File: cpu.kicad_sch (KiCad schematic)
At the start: 17 parts, among them J1 FTSH-105-01-L-DV-K, U2 CC1312R1F3RGZR, Y2 OW7EL89CANUXK7YLC-48M

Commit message: Finish up inputting things
Signed-off-by: Corey Minyard <corey@minyard.net>
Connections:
- net 144MHz_TX_ENABLE: now reaches U2.28 (DIO_18)
- net 440MHz_TX_ENABLE: now reaches U2.29 (DIO_19)
- no-connect marks 16 -> 14
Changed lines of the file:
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@@
-	)
-	(no_connect
-		(at 78.74 95.25)
 	)
 	(no_connect
@@
 	)
 	(no_connect
-		(at 78.74 97.79)
-	)
-	(no_connect
 		(at 78.74 110.49)
 	)
@@
 	(wire
 		(pts
-			(xy 63.5 123.19) (xy 78.74 123.19)
+			(xy 62.23 123.19) (xy 78.74 123.19)
 		)
 		(stroke
@@
 	(wire
 		(pts
+			(xy 59.69 97.79) (xy 78.74 97.79)
+		)
+		(stroke
+			(width 0)
+			(type default)
+		)
+	)
+	(wire
+		(pts
 			(xy 57.15 153.67) (xy 62.23 153.67)
 		)
@@
 		(pts
 			(xy 139.7 52.07) (xy 148.59 52.07)
+		)
+		(stroke
+			(width 0)
+			(type default)
+		)
+	)
+	(wire
+		(pts
+			(xy 59.69 95.25) (xy 78.74 95.25)
 		)
 		(stroke
@@
 		)
 	)
+	(global_label "144MHz_TX_ENABLE"
+		(shape input)
+		(at 59.69 95.25 180)
+		(fields_autoplaced yes)
+		(effects
+			(font
+				(size 1.27 1.27)
+			)
+			(justify right)
+		)
+		(property "Intersheetrefs" "${INTERSHEET_REFS}"
+			(at 38.1388 95.25 0)
+			(effects
+				(font
+					(size 1.27 1.27)
+				)
+				(justify right)
+				(hide yes)
+			)
+		)
+	)
 	(global_label "144MHz_RF_P"
 		(shape input)
@@
 	(global_label "RADIO2_TCXO_POW"
 		(shape input)
-		(at 63.5 123.19 180)
+		(at 62.23 123.19 180)
 		(fields_autoplaced yes)
 		(effects
@@
 		)
 		(property "Intersheetrefs" "${INTERSHEET_REFS}"
-			(at 42.9767 123.19 0)
+			(at 41.7067 123.19 0)
 			(effects
 				(font
@@
 		(property "Intersheetrefs" "${INTERSHEET_REFS}"
 			(at 41.8882 85.09 0)
+			(effects
+				(font
+					(size 1.27 1.27)
+				)
+				(justify right)
+				(hide yes)
+			)
+		)
+	)
+	(global_label "440MHz_TX_ENABLE"
+		(shape input)
+		(at 59.69 97.79 180)
+		(fields_autoplaced yes)
+		(effects
+			(font
+				(size 1.27 1.27)
+			)
+			(justify right)
+		)
+		(property "Intersheetrefs" "${INTERSHEET_REFS}"
+			(at 38.1388 97.79 0)
 			(effects
 				(font
@@
 		(dnp no)
 		(property "Reference" "C8"
-			(at 150.876 131.826 90)
+			(at 153.416 129.54 90)
 			(effects
 				(font
@@
 		)
 		(property "Value" "1nF"
-			(at 160.02 132.08 90)
-			(effects
-				(font
+			(at 154.432 137.414 90)
+			(effects
+				(font

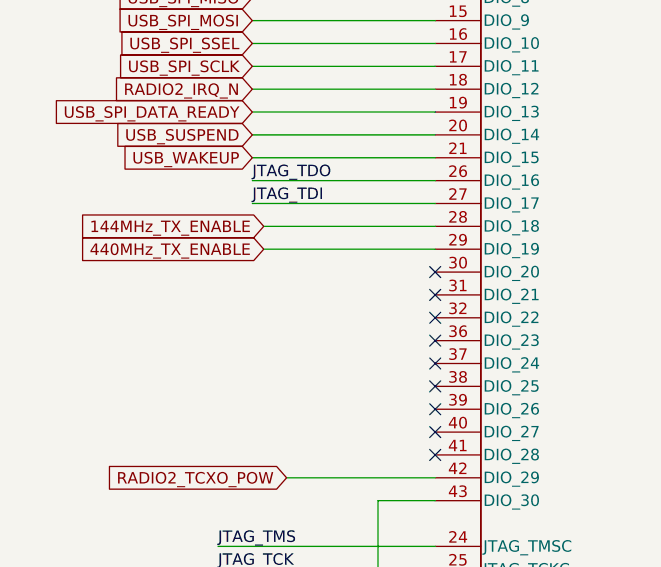
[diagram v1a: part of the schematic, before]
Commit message: Clean up schematics
Signed-off-by: Corey Minyard <corey@minyard.net>
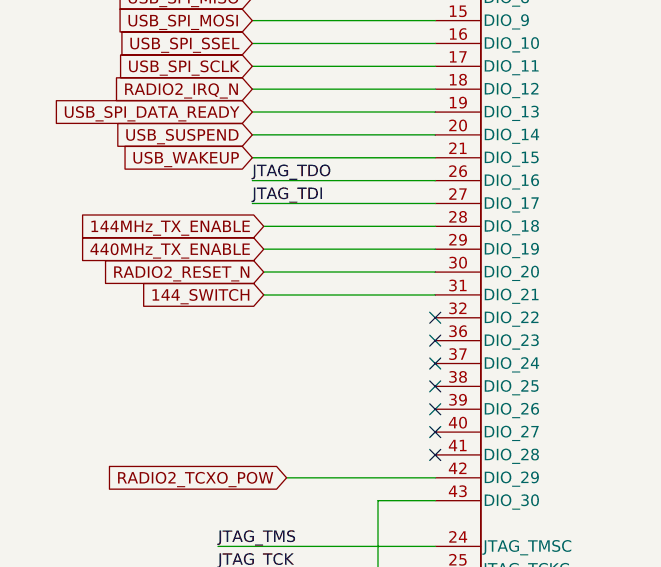
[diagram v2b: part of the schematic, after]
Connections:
- net RADIO2_RESET_N: now reaches U2.30 (DIO_20)
- net 144_SWITCH: now reaches U2.31 (DIO_21)
- no-connect marks 14 -> 12
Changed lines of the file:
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@@
 	)
 	(no_connect
-		(at 78.74 100.33)
-	)
-	(no_connect
 		(at 139.7 162.56)
 	)
@@
 	)
 	(no_connect
-		(at 78.74 102.87)
-	)
-	(no_connect
 		(at 78.74 115.57)
 	)
@@
 	(wire
 		(pts
+			(xy 59.69 102.87) (xy 78.74 102.87)
+		)
+		(stroke
+			(width 0)
+			(type default)
+		)
+	)
+	(wire
+		(pts
 			(xy 165.1 69.85) (xy 182.88 69.85)
 		)
@@
 	(wire
 		(pts
+			(xy 59.69 100.33) (xy 78.74 100.33)
+		)
+		(stroke
+			(width 0)
+			(type default)
+		)
+	)
+	(wire
+		(pts
 			(xy 58.42 67.31) (xy 78.74 67.31)
 		)
@@
 		)
 	)
+	(global_label "RADIO2_RESET_N"
+		(shape input)
+		(at 59.69 100.33 180)
+		(fields_autoplaced yes)
+		(effects
+			(font
+				(size 1.27 1.27)
+			)
+			(justify right)
+		)
+		(property "Intersheetrefs" "${INTERSHEET_REFS}"
+			(at 40.9206 100.33 0)
+			(effects
+				(font
+					(size 1.27 1.27)
+				)
+				(justify right)
+				(hide yes)
+			)
+		)
+	)
 	(global_label "USB_SPI_MOSI"
 		(shape input)
@@
 		)
 	)
+	(global_label "144_SWITCH"
+		(shape input)
+		(at 59.69 102.87 180)
+		(fields_autoplaced yes)
+		(effects
+			(font
+				(size 1.27 1.27)
+			)
+			(justify right)
+		)
+		(property "Intersheetrefs" "${INTERSHEET_REFS}"
+			(at 45.2749 102.87 0)
+			(effects
+				(font
+					(size 1.27 1.27)
+				)
+				(justify right)
+				(hide yes)
+			)
+		)
+	)
 	(global_label "USB_WAKEUP"
 		(shape input)
@@
 		(pin "22"
 		)
+		(instances
+			(project ""
+				(path "/23e49ab9-97e0-460a-806c-ff6f37958474/f1de8cbf-f219-47ea-9542-15169289ddba"
+					(reference "U2")
+					(unit 1)
+				)
+			)
+		)
 	)

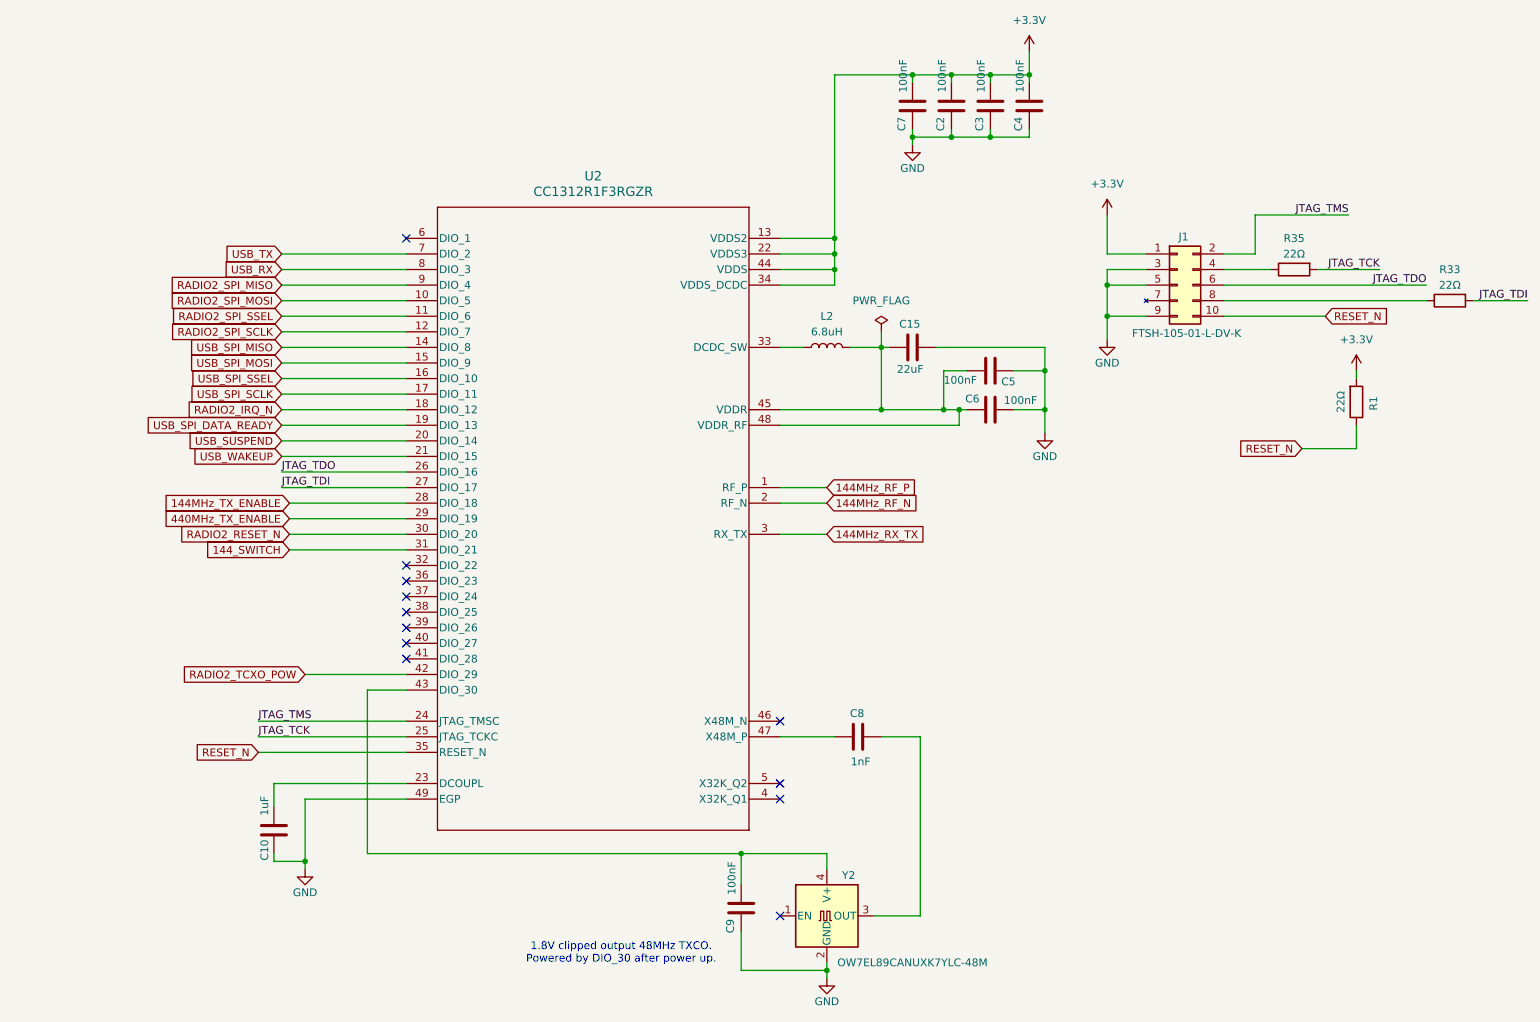
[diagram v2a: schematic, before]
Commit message: More cleanups and add some test points
Signed-off-by: Corey Minyard <corey@minyard.net>
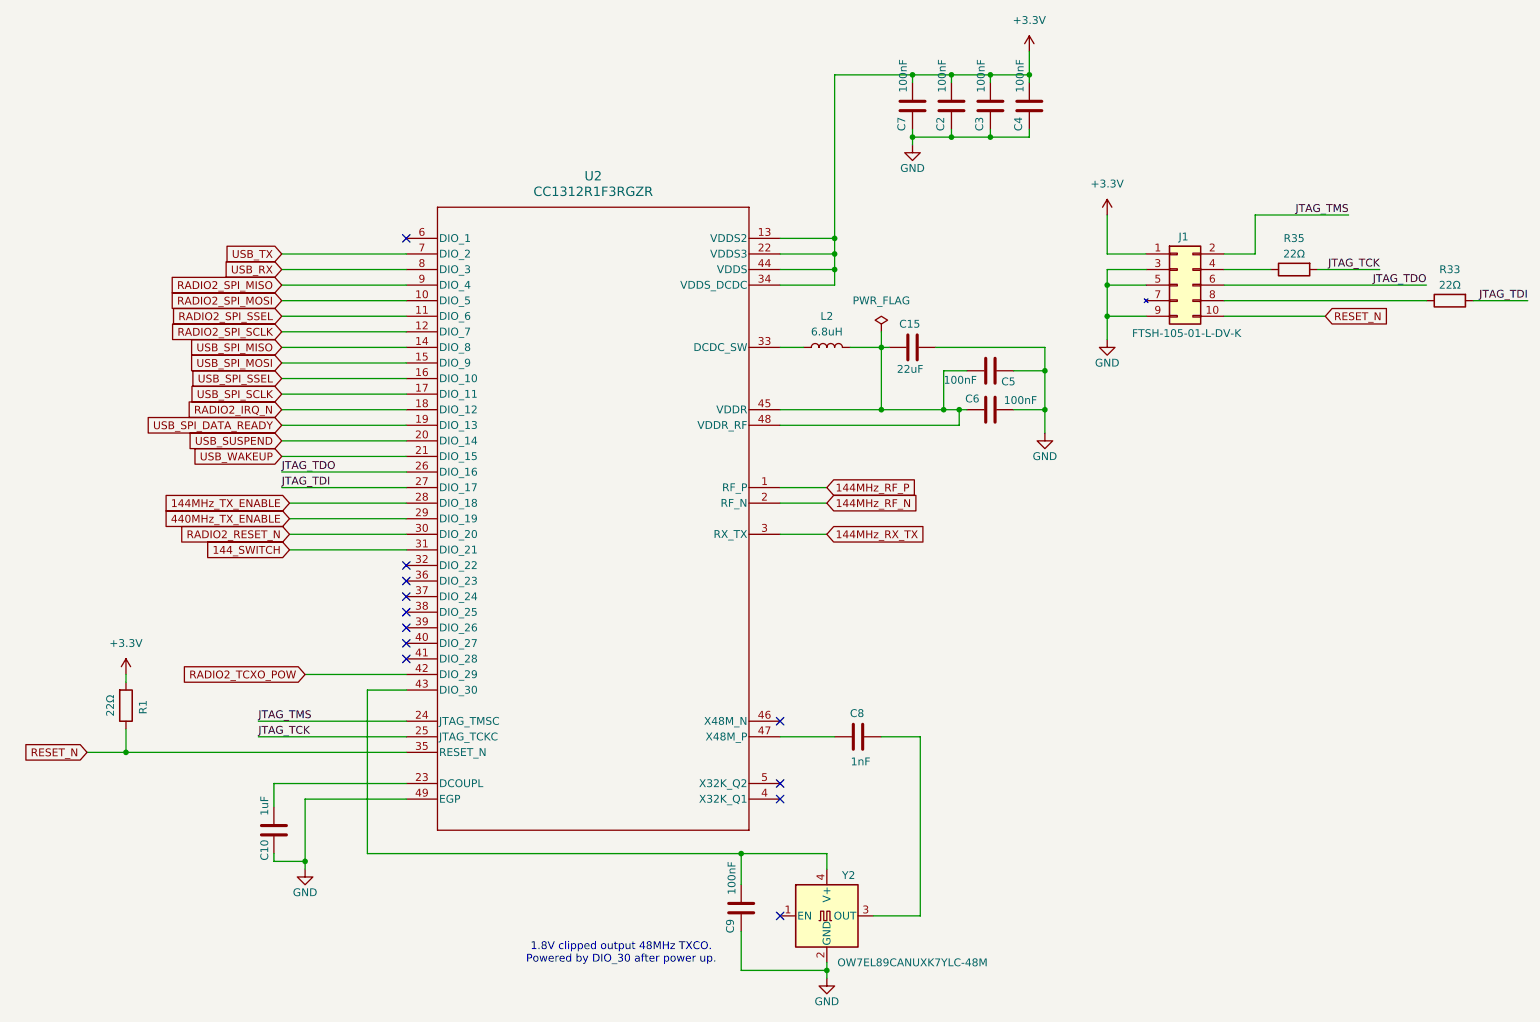
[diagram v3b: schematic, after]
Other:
- moved on the sheet: R1
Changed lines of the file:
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@@
+	)
+	(junction
+		(at 33.02 135.89)
+		(diameter 0)
+		(color 0 0 0 0)
 	)
 	(junction
@@
 	(wire
 		(pts
-			(xy 54.61 135.89) (xy 78.74 135.89)
+			(xy 26.67 135.89) (xy 33.02 135.89)
 		)
 		(stroke
@@
 	(wire
 		(pts
+			(xy 33.02 132.08) (xy 33.02 135.89)
+		)
+		(stroke
+			(width 0)
+			(type default)
+		)
+	)
+	(wire
+		(pts
 			(xy 173.99 25.4) (xy 167.64 25.4)
 		)
@@
 	(wire
 		(pts
-			(xy 224.79 86.36) (xy 233.68 86.36)
-		)
-		(stroke
-			(width 0)
-			(type default)
-		)
-	)
-	(wire
-		(pts
 			(xy 139.7 95.25) (xy 147.32 95.25)
 		)
@@
 	(wire
 		(pts
-			(xy 233.68 82.55) (xy 233.68 86.36)
-		)
-		(stroke
-			(width 0)
-			(type default)
-		)
-	)
-	(wire
-		(pts
 			(xy 58.42 72.39) (xy 78.74 72.39)
 		)
@@
 	(wire
 		(pts
-			(xy 233.68 73.66) (xy 233.68 74.93)
-		)
-		(stroke
-			(width 0)
-			(type default)
-		)
-	)
-	(wire
-		(pts
 			(xy 166.37 80.01) (xy 166.37 73.66)
 		)
@@
 	(wire
 		(pts
+			(xy 33.02 135.89) (xy 78.74 135.89)
+		)
+		(stroke
+			(width 0)
+			(type default)
+		)
+	)
+	(wire
+		(pts
 			(xy 147.32 170.18) (xy 147.32 171.45)
 		)
@@
 		(pts
 			(xy 217.17 54.61) (xy 212.09 54.61)
+		)
+		(stroke
+			(width 0)
+			(type default)
+		)
+	)
+	(wire
+		(pts
+			(xy 33.02 123.19) (xy 33.02 124.46)
 		)
 		(stroke
@@
 	(global_label "RESET_N"
 		(shape input)
-		(at 54.61 135.89 180)
+		(at 26.67 135.89 180)
 		(fields_autoplaced yes)
 		(effects
@@
 		)
 		(property "Intersheetrefs" "${INTERSHEET_REFS}"
-			(at 43.5816 135.89 0)
+			(at 15.6416 135.89 0)
 			(effects
 				(font
@@
 		(property "Intersheetrefs" "${INTERSHEET_REFS}"
 			(at 42.1904 80.01 0)
-			(effects
-				(font
-					(size 1.27 1.27)
-				)
-				(justify right)
-				(hide yes)
-			)
-		)
-	)
-	(global_label "RESET_N"
-		(shape input)
-		(at 224.79 86.36 180)
-		(fields_autoplaced yes)
-		(effects
-			(font
-				(size 1.27 1.27)
-			)
-			(justify right)
-		)
-		(property "Intersheetrefs" "${INTERSHEET_REFS}"
-			(at 213.7616 86.36 0)
 			(effects
 				(font
@@
 	(symbol
 		(lib_id "Device:R")
-		(at 233.68 78.74 0)
+		(at 33.02 128.27 0)
 		(mirror x)
 		(unit 1)
@@
 		(dnp no)
 		(property "Reference" "R1"
-			(at 236.474 78.994 90)
+			(at 35.814 128.524 90)
 			(effects
 				(font
@@
 		)
 		(property "Value" "22Ω"
-			(at 231.14 78.74 90)
+			(at 30.48 128.27 90)
 			(effects
 				(font
@@
 		)
 		(property "Footprint" "Resistor_SMD:R_0402_1005Metric"
-			(at 231.902 78.74 90)
+			(at 31.242 128.27 90)
 			(effects
 				(font
@@
 		)
 		(property "Datasheet" "~"
-			(at 233.68 78.74 0)
+			(at 33.02 128.27 0)
 			(effects
 				(font
@@
 		)
 		(property "Description" "Resistor"
-			(at 233.68 78.74 0)
+			(at 33.02 128.27 0)
 			(effects
 				(font
@@
 	(symbol
 		(lib_id "power:+3.3V")
-		(at 233.68 73.66 0)
+		(at 33.02 123.19 0)
 		(unit 1)
 		(exclude_from_sim no)
@@
 		(fields_autoplaced yes)
 		(property "Reference" "#PWR06"
-			(at 233.68 77.47 0)
+			(at 33.02 127 0)
 			(effects
 				(font
@@
 		)
 		(property "Value" "+3.3V"
-			(at 233.68 68.58 0)
+			(at 33.02 118.11 0)
 			(effects
 				(font
@@
 		)
 		(property "Footprint" ""
-			(at 233.68 73.66 0)
+			(at 33.02 123.19 0)
 			(effects
 				(font
@@
 		)
 		(property "Datasheet" ""
-			(at 233.68 73.66 0)
+			(at 33.02 123.19 0)
 			(effects
 				(font
@@
 		)
 		(property "Description" "Power symbol creates a global label with name \"+3.3V\""
-			(at 233.68 73.66 0)
-			(effects
-				(font
+			(at 33.02 123.19 0)
+			(effects
+				(font

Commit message: Finish layout
Signed-off-by: Corey Minyard <corey@minyard.net>
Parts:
- added J24: HTSW-103-07-G-S, CON3_1X3_TU_TSW, symbol Local Connectors:HTSW-103-07-G-S
- added R20: 22Ω, Resistor_SMD:R_0402_1005Metric, symbol Device:R
- R1: value 22Ω -> 10K
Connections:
- net 144MHz_TX_ENABLE: now also U2.10 (DIO_5); no longer U2.28 (DIO_18)
- net 144_SWITCH: now also U2.9 (DIO_4); no longer U2.31 (DIO_21)
- net 440MHz_TX_ENABLE: now also U2.6 (DIO_1); no longer U2.29 (DIO_19)
- net GND: now also J24.3
- net RADIO2_IRQ_N: now also U2.29 (DIO_19); no longer U2.18 (DIO_12)
- net RADIO2_SPI_MISO: now also U2.19 (DIO_13); no longer U2.9 (DIO_4)
- net RADIO2_SPI_MOSI: now also U2.21 (DIO_15); no longer U2.10 (DIO_5)
- net RADIO2_SPI_SCLK: now also R20.1; no longer U2.12 (DIO_7)
- net RADIO2_SPI_SSEL: now also U2.18 (DIO_12); no longer U2.11 (DIO_6)
- net USB_RX: now also J24.1
- net USB_SPI_DATA_READY: now also U2.28 (DIO_18); no longer U2.19 (DIO_13)
- net USB_SUSPEND: now also U2.12 (DIO_7); no longer U2.20 (DIO_14)
- net USB_TX: now also J24.2
- net USB_WAKEUP: now also U2.11 (DIO_6); no longer U2.21 (DIO_15)
- new net: R20.2, U2.20 (DIO_14)

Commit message: Reduce hole sizes and add more holes on PA
Meet spec requirements.

Signed-off-by: Corey Minyard <corey@minyard.net>
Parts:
- J24: footprint CON3_1X3_TU_TSW -> footprints:CON3_1X3_TU_TSW
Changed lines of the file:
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@@
 			)
 		)
-		(property "Footprint" "CON3_1X3_TU_TSW"
+		(property "Footprint" "footprints:CON3_1X3_TU_TSW"
 			(at 219.456 95.504 0)
 			(effects

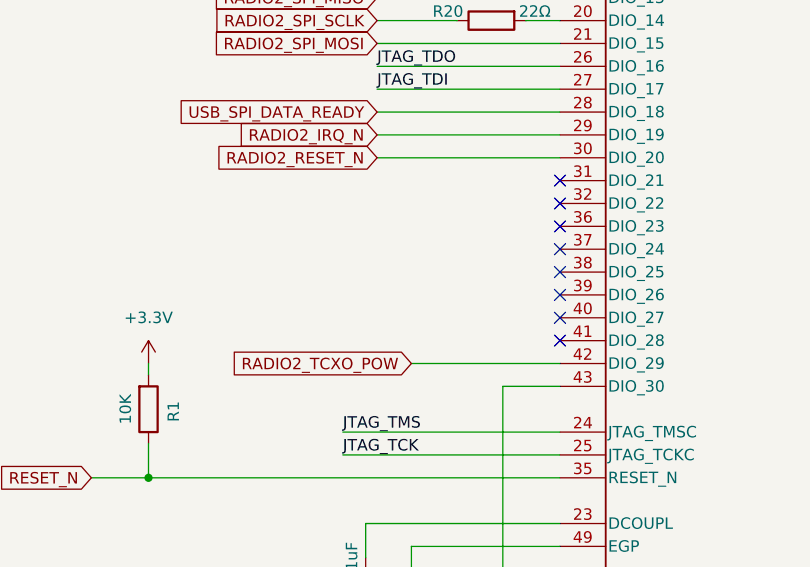
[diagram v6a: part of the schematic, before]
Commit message: Add fiduciaries and a control output
Signed-off-by: Corey Minyard <corey@minyard.net>
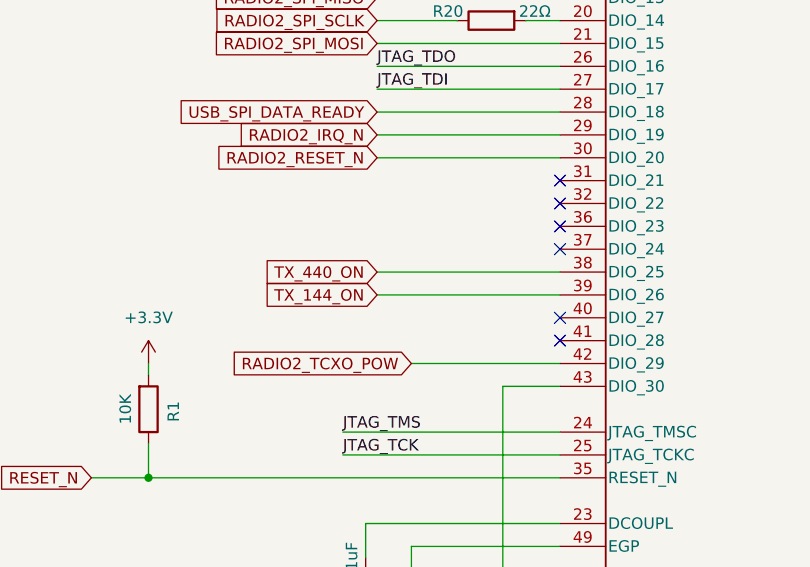
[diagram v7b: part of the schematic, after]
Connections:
- net TX_440_ON: now reaches U2.38 (DIO_25)
- net TX_144_ON: now reaches U2.39 (DIO_26)
- no-connect marks 12 -> 10
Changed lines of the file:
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@@
-	)
-	(no_connect
-		(at 78.74 113.03)
 	)
 	(no_connect
@@
 	)
 	(no_connect
-		(at 78.74 115.57)
-	)
-	(no_connect
 		(at 78.74 102.87)
 	)
@@
 	(wire
 		(pts
+			(xy 58.42 113.03) (xy 78.74 113.03)
+		)
+		(stroke
+			(width 0)
+			(type default)
+		)
+	)
+	(wire
+		(pts
 			(xy 180.34 21.59) (xy 180.34 25.4)
 		)
@@
 		(pts
 			(xy 182.88 69.85) (xy 182.88 73.66)
+		)
+		(stroke
+			(width 0)
+			(type default)
+		)
+	)
+	(wire
+		(pts
+			(xy 58.42 115.57) (xy 78.74 115.57)
 		)
 		(stroke
@@
 		)
 	)
+	(global_label "TX_440_ON"
+		(shape input)
+		(at 58.42 113.03 180)
+		(fields_autoplaced yes)
+		(effects
+			(font
+				(size 1.27 1.27)
+			)
+			(justify right)
+		)
+		(property "Intersheetrefs" "${INTERSHEET_REFS}"
+			(at 45.033 113.03 0)
+			(effects
+				(font
+					(size 1.27 1.27)
+				)
+				(justify right)
+				(hide yes)
+			)
+		)
+	)
 	(global_label "440MHz_TX_ENABLE"
 		(shape input)
@@
 			(effects
 				(font
+					(size 1.27 1.27)
+				)
+				(justify right)
+				(hide yes)
+			)
+		)
+	)
+	(global_label "TX_144_ON"
+		(shape input)
+		(at 58.42 115.57 180)
+		(fields_autoplaced yes)
+		(effects
+			(font
+				(size 1.27 1.27)
+			)
+			(justify right)
+		)
+		(property "Intersheetrefs" "${INTERSHEET_REFS}"
+			(at 45.033 115.57 0)
+			(effects
+				(font
